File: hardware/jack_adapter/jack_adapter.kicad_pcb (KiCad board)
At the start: 2 copper layers, 25.8 x 22.5 mm, 7 parts, among them J1 2.5mm Mic, J3 3.5mm Headphones, J4 Header

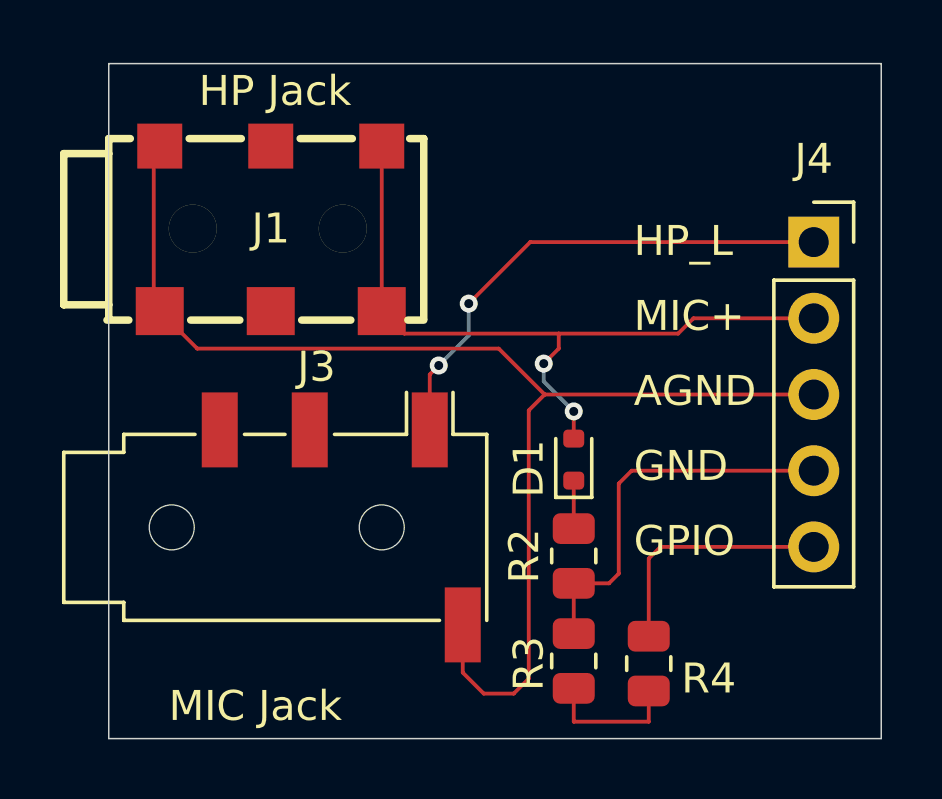
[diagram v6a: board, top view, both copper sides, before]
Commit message: bugfix: updated the footprint to be what it actually is a TRRS and match what the datasheet says. As well, updated the sch to match that it is a TRRS
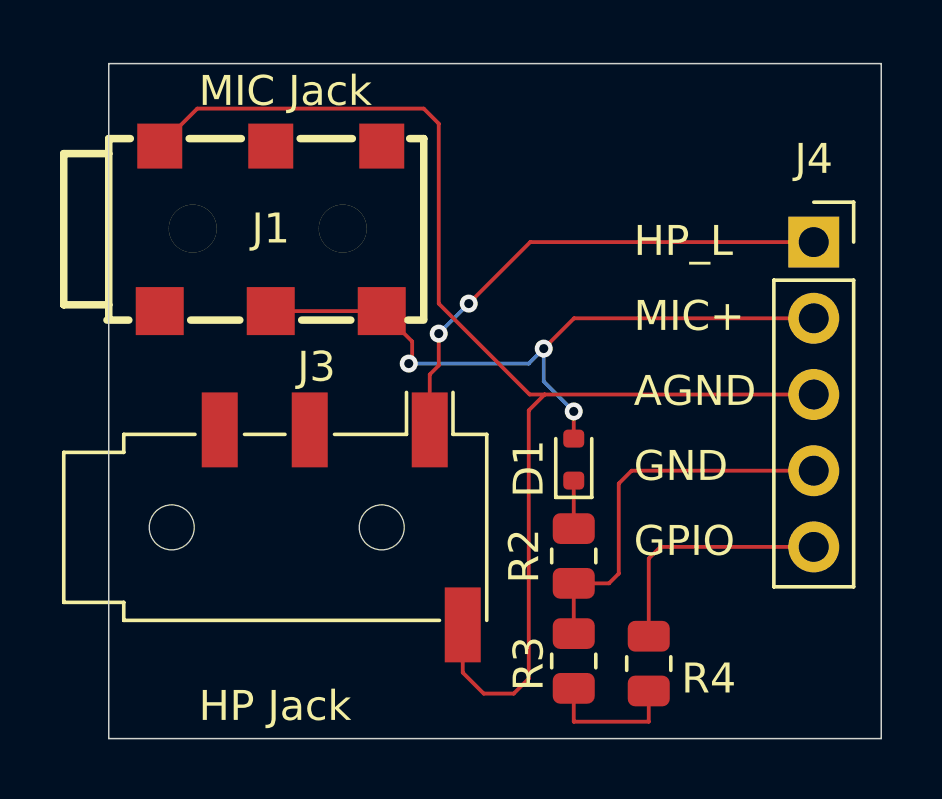
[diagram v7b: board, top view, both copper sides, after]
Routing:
- net Net-(D1-A): track 24.7 -> 23.5 mm, vias 2 -> 3
- net Net-(J4-Pin_3): track 42.8 -> 43.9 mm

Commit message: bugfix: cleanup the schematic and pcb
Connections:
- J3 pad R1: (no net) -> unconnected-(J3-PadR1)
- J3 pad R2: (no net) -> unconnected-(J3-PadR2)
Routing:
- net Net-(J4-Pin_3): track 43.9 -> 45.1 mm
- net Net-(D1-A): track 23.5 -> 22.9 mm, vias 3 -> 4
